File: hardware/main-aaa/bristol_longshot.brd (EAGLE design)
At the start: 14 x 50 mm, 57 parts, among them U1 SAM_D20E, U2 SI4060, U3 UBLOX_MAX, U4 ADP1607ACPZN-R7, U5 TG-5006CJ, U6 TG-5006CJ, U7 TPS3123, U8 SN74LVC1G32DCKR, U9 SE880, Y1 ABS05

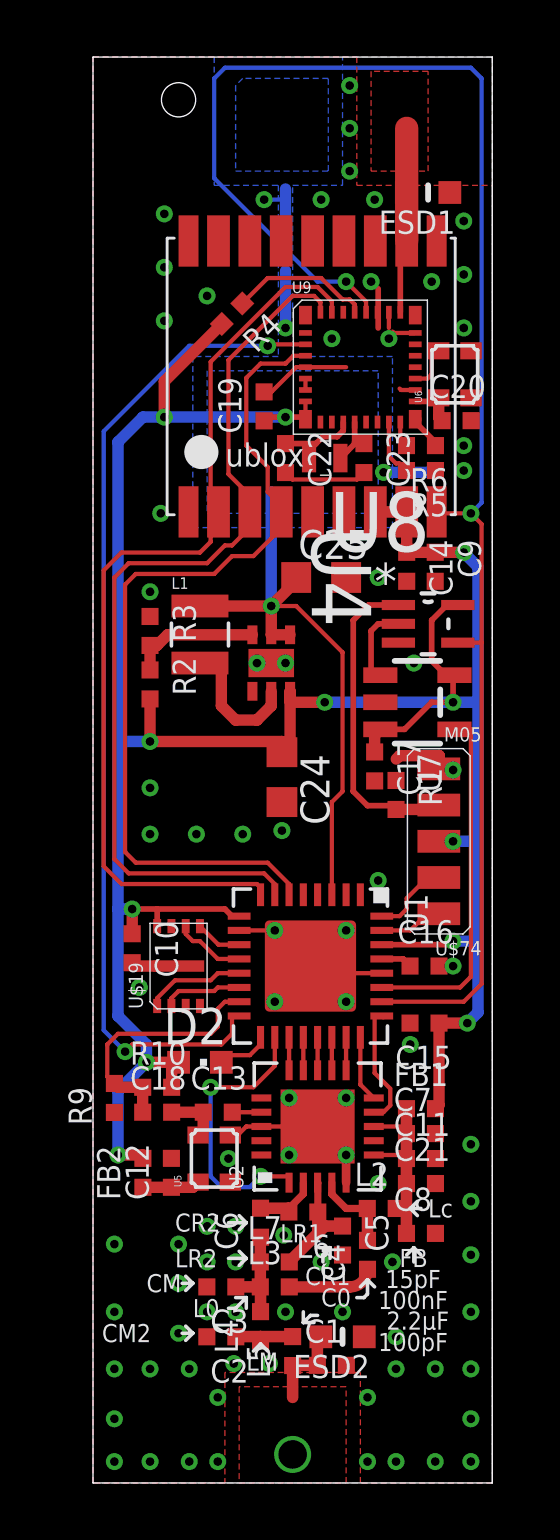
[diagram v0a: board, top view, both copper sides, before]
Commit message: Updated many parts lists, updated bard numbering, removed makefiles for inactive things
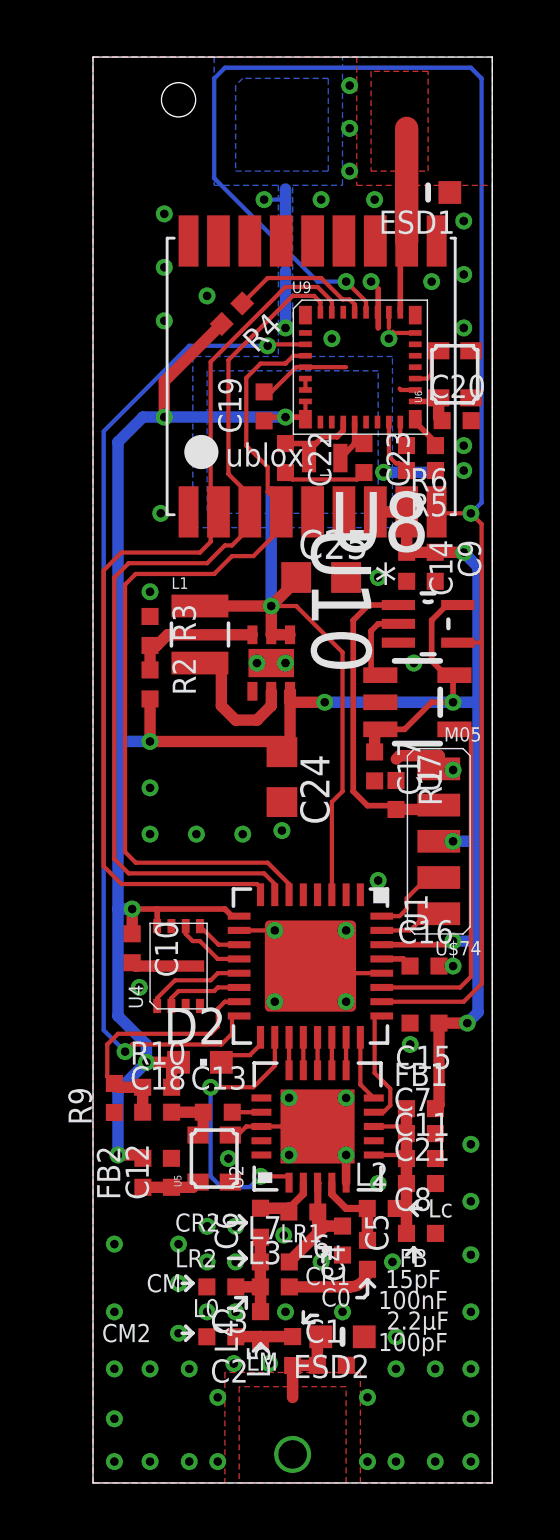
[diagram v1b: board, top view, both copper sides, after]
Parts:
- removed U$19: SST25WF040BT-40I/NP, fbri:USON-8
- added U10: ADP1607ACPZN-R7, ADP1607:DFN200X200X60-7N
- U4: value ADP1607ACPZN-R7 -> SST25WF040BT-40I/NP; device ADP1607:DFN200X200X60-7N -> fbri:USON-8
- moved U4 11.1 mm to (3.00, 18.1), turned to 0 degrees
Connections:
- net 1.2V: now also U10.1, U10.2; no longer U4.1, U4.2
- net 1.8V: now also U10.6, U4.8; no longer U$19.8, U4.6
- net FB: now also U10.3; no longer U4.3
- net GND: now also U10.4, U10.7, U4.P$9; no longer U$19.4, U$19.P$9, U4.7
- net MEM_CSN: now also U4.1; no longer U$19.1
- net MEM_MISO: now also U4.2; no longer U$19.2
- net MEM_MOSI: now also U4.5; no longer U$19.5
- net MEM_SCK: now also U4.6; no longer U$19.6
- net MEM_WPN: now also U4.3; no longer U$19.3
- net SW: now also U10.5; no longer U4.5
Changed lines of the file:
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@@
 <element name="C20" library="microbuilder_v3" package="_0402" value="100nF" x="12.75" y="37.25"/>
 <element name="C17" library="microbuilder_v3" package="_0402" value="100nF" x="9.875" y="25.125" rot="R270"/>
-<element name="U$19" library="fbri" package="USON-8" value="SST25WF040BT-40I/NP" x="3" y="18.125"/>
+<element name="U4" library="fbri" package="USON-8" value="SST25WF040BT-40I/NP" x="3" y="18.125"/>
 <element name="L1" library="SparkFun" package="1007" value="2.2µH" x="3.75" y="29.75"/>
 <element name="C24" library="resistor" package="C0603K" value="10µF" x="6.625" y="24.75" rot="R270"/>
-<element name="U4" library="ADP1607" package="DFN200X200X60-7N" value="ADP1607ACPZN-R7" x="6.25" y="28.75" rot="R270">
+<element name="U10" library="ADP1607" package="DFN200X200X60-7N" value="ADP1607ACPZN-R7" x="6.25" y="28.75" rot="R270">
 <attribute name="OC_FARNELL" value="2254940" x="51.25" y="39.75" size="1.778" layer="27" rot="R270" display="off"/>
 <attribute name="OC_NEWARK" value="54W6610" x="51.25" y="39.75" size="1.778" layer="27" rot="R270" display="off"/>
@@
 <via x="9" y="49" extent="1-16" drill="0.3"/>
 <via x="9" y="47.5" extent="1-16" drill="0.3"/>
-<contactref element="U$19" pad="4"/>
-<contactref element="U$19" pad="P$9"/>
+<contactref element="U4" pad="4"/>
+<contactref element="U4" pad="P$9"/>
 <via x="1.625" y="17.375" extent="1-16" drill="0.3"/>
 <wire x1="2.25" y1="18.125" x2="1.5" y2="18.125" width="0.4" layer="1"/>
 <wire x1="1.5" y1="18.125" x2="1.383" y2="18.242" width="0.4" layer="1"/>
 <wire x1="1.383" y1="18.242" x2="1.375" y2="18.242" width="0.4" layer="1"/>
-<contactref element="U4" pad="4"/>
+<contactref element="U10" pad="4"/>
 <contactref element="C24" pad="2"/>
-<contactref element="U4" pad="7"/>
+<contactref element="U10" pad="7"/>
 <contactref element="R3" pad="1"/>
 <contactref element="C25" pad="2"/>
@@
 <wire x1="9.875" y1="26.2251" x2="9.875" y2="25.633" width="0.4" layer="1"/>
 <via x="13" y="32.625" extent="1-16" drill="0.3"/>
-<contactref element="U$19" pad="8"/>
+<contactref element="U4" pad="8"/>
 <wire x1="1.375" y1="20.125" x2="2.25" y2="20.125" width="0.2" layer="1"/>
 <wire x1="2.25" y1="20.125" x2="4.625" y2="20.125" width="0.2" layer="1"/>
@@
 <wire x1="0.875" y1="13.75" x2="1.875" y2="14.75" width="0.4" layer="16"/>
 <contactref element="C24" pad="1"/>
-<contactref element="U4" pad="6"/>
+<contactref element="U10" pad="6"/>
 <contactref element="R2" pad="2"/>
 <via x="8.125" y="27.375" extent="1-16" drill="0.3"/>
@@
 </signal>
 <signal name="MEM_MOSI">
-<contactref element="U$19" pad="5"/>
+<contactref element="U4" pad="5"/>
 <contactref element="U1" pad="11"/>
 <wire x1="5.125" y1="18.875" x2="4.4" y2="18.875" width="0.15" layer="1"/>
@@
 </signal>
 <signal name="MEM_CSN">
-<contactref element="U$19" pad="1"/>
+<contactref element="U4" pad="1"/>
 <contactref element="U1" pad="13"/>
 <wire x1="5.125" y1="17.875" x2="4.375" y2="17.875" width="0.15" layer="1"/>
@@
 </signal>
 <signal name="MEM_SCK">
-<contactref element="U$19" pad="6"/>
+<contactref element="U4" pad="6"/>
 <contactref element="U1" pad="12"/>
 <wire x1="5.125" y1="18.375" x2="4.375" y2="18.375" width="0.15" layer="1"/>
@@
 </signal>
 <signal name="MEM_MISO">
-<contactref element="U$19" pad="2"/>
+<contactref element="U4" pad="2"/>
 <contactref element="U1" pad="14"/>
 <wire x1="5.125" y1="17.375" x2="4.375" y2="17.375" width="0.15" layer="1"/>
@@
 </signal>
 <signal name="MEM_WPN">
-<contactref element="U$19" pad="3"/>
+<contactref element="U4" pad="3"/>
 </signal>
 <signal name="RF_TANK">
@@
 </signal>
 <signal name="1.2V">
-<contactref element="U4" pad="1"/>
-<contactref element="U4" pad="2"/>
+<contactref element="U10" pad="1"/>
+<contactref element="U10" pad="2"/>
 <contactref element="L1" pad="1"/>
 <contactref element="C25" pad="1"/>
@@
 </signal>
 <signal name="SW">
-<contactref element="U4" pad="5"/>
+<contactref element="U10" pad="5"/>
 <contactref element="L1" pad="2"/>
 <wire x1="3.75" y1="28.75" x2="3.875" y2="28.625" width="0.4" layer="1"/>
@@
 </signal>
 <signal name="FB">
-<contactref element="U4" pad="3"/>
+<contactref element="U10" pad="3"/>
 <contactref element="R3" pad="2"/>
 <contactref element="R2" pad="1"/>

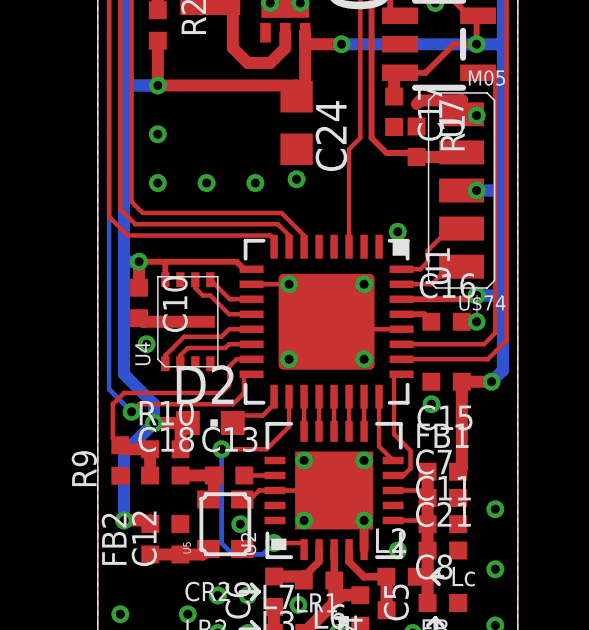
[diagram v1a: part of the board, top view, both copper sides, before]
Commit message: [Bugfix] Memory HOLD pin needs to be high. Also adjusted pad/cream size. Bump to V0.98x.1
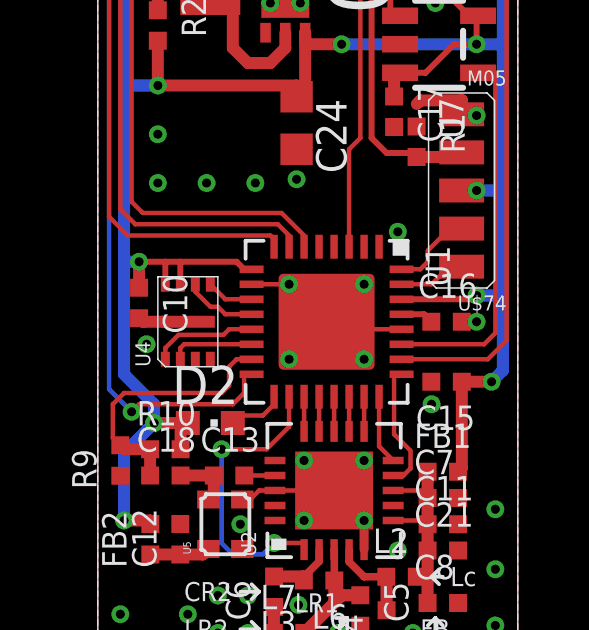
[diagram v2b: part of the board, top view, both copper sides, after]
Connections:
- net 1.8V: now also U4.7
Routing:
- net 1.8V: track 103.6 -> 104.5 mm
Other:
- board text added: "V0.982.1"
- board text removed: "V0.982.0"
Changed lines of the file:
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@@
 <wire x1="1.625" y1="48.875" x2="0.625" y2="49.375" width="0.2" layer="29" curve="-75"/>
 <wire x1="1.625" y1="41.875" x2="0.625" y2="41.375" width="0.2" layer="29"/>
-<text x="2.25" y="45.75" size="0.8" layer="29" font="vector" ratio="14">V0.982.0</text>
+<text x="2.25" y="45.75" size="0.8" layer="29" font="vector" ratio="14">V0.982.1</text>
 <rectangle x1="4.5" y1="45.5" x2="9" y2="49.5" layer="40"/>
 <rectangle x1="3.5" y1="33.5" x2="10.5" y2="39.5" layer="40"/>
@@
 <contactref element="U4" pad="8"/>
 <wire x1="1.375" y1="20.125" x2="2.25" y2="20.125" width="0.2" layer="1"/>
-<wire x1="2.25" y1="20.125" x2="4.625" y2="20.125" width="0.2" layer="1"/>
+<wire x1="2.25" y1="20.125" x2="2.75" y2="20.125" width="0.2" layer="1"/>
+<wire x1="2.75" y1="20.125" x2="4.625" y2="20.125" width="0.2" layer="1"/>
 <wire x1="4.625" y1="20.125" x2="4.875" y2="19.875" width="0.2" layer="1"/>
 <wire x1="4.875" y1="19.875" x2="5.125" y2="19.875" width="0.2" layer="1"/>
-<wire x1="2.25" y1="19.525" x2="2.25" y2="20.125" width="0.2" layer="1"/>
+<wire x1="2.25" y1="19.375" x2="2.25" y2="20.125" width="0.2" layer="1"/>
 <wire x1="1.375" y1="19.258" x2="1.375" y2="20.125" width="0.4" layer="1"/>
 <wire x1="2.5" y1="38.625" x2="4.5157875" y2="40.6407875" width="0.4" layer="1"/>
@@
 <wire x1="2" y1="26" x2="6.625" y2="26" width="0.4" layer="1"/>
 <wire x1="6.625" y1="26" x2="6.625" y2="25.625" width="0.4" layer="1"/>
+<contactref element="U4" pad="7"/>
+<wire x1="2.75" y1="19.375" x2="2.75" y2="20.125" width="0.2" layer="1"/>
 </signal>
 <signal name="VDD_CORE">
@@
 <contactref element="U4" pad="5"/>
 <contactref element="U1" pad="11"/>
-<wire x1="5.125" y1="18.875" x2="4.4" y2="18.875" width="0.15" layer="1"/>
-<wire x1="4.4" y1="18.875" x2="3.75" y2="19.525" width="0.15" layer="1"/>
+<wire x1="5.125" y1="18.875" x2="4.25" y2="18.875" width="0.15" layer="1"/>
+<wire x1="4.25" y1="18.875" x2="3.75" y2="19.375" width="0.15" layer="1"/>
 </signal>
 <signal name="MEM_CSN">
@@
 <contactref element="U1" pad="13"/>
 <wire x1="5.125" y1="17.875" x2="4.375" y2="17.875" width="0.15" layer="1"/>
-<wire x1="4.375" y1="17.875" x2="4.125" y2="17.625" width="0.15" layer="1"/>
-<wire x1="4.125" y1="17.625" x2="2.875" y2="17.625" width="0.15" layer="1"/>
-<wire x1="2.875" y1="17.625" x2="2.25" y2="17" width="0.15" layer="1"/>
-<wire x1="2.25" y1="17" x2="2.25" y2="16.725" width="0.15" layer="1"/>
+<wire x1="4.375" y1="17.875" x2="4.1875" y2="17.6875" width="0.15" layer="1"/>
+<wire x1="4.1875" y1="17.6875" x2="2.6875" y2="17.6875" width="0.15" layer="1"/>
+<wire x1="2.6875" y1="17.6875" x2="2.25" y2="17.25" width="0.15" layer="1"/>
+<wire x1="2.25" y1="17.25" x2="2.25" y2="16.875" width="0.15" layer="1"/>
 </signal>
 <signal name="GIMO">
@@
 <contactref element="U4" pad="6"/>
 <contactref element="U1" pad="12"/>
-<wire x1="5.125" y1="18.375" x2="4.375" y2="18.375" width="0.15" layer="1"/>
-<wire x1="4.375" y1="18.375" x2="3.75" y2="19" width="0.15" layer="1"/>
-<wire x1="3.75" y1="19" x2="3.5" y2="19" width="0.15" layer="1"/>
-<wire x1="3.5" y1="19" x2="3.25" y2="19.25" width="0.15" layer="1"/>
-<wire x1="3.25" y1="19.25" x2="3.25" y2="19.525" width="0.15" layer="1"/>
+<wire x1="5.125" y1="18.375" x2="4.25" y2="18.375" width="0.15" layer="1"/>
+<wire x1="4.25" y1="18.375" x2="4" y2="18.625" width="0.15" layer="1"/>
+<wire x1="4" y1="18.625" x2="3.75" y2="18.625" width="0.15" layer="1"/>
+<wire x1="3.75" y1="18.625" x2="3.25" y2="19.125" width="0.15" layer="1"/>
+<wire x1="3.25" y1="19.125" x2="3.25" y2="19.375" width="0.15" layer="1"/>
 </signal>
 <signal name="MEM_MISO">
 <contactref element="U4" pad="2"/>
 <contactref element="U1" pad="14"/>
-<wire x1="5.125" y1="17.375" x2="4.375" y2="17.375" width="0.15" layer="1"/>
-<wire x1="4.375" y1="17.375" x2="4.25" y2="17.25" width="0.15" layer="1"/>
-<wire x1="4.25" y1="17.25" x2="3" y2="17.25" width="0.15" layer="1"/>
-<wire x1="3" y1="17.25" x2="2.75" y2="17" width="0.15" layer="1"/>
-<wire x1="2.75" y1="17" x2="2.75" y2="16.725" width="0.15" layer="1"/>
+<wire x1="5.125" y1="17.375" x2="2.875" y2="17.375" width="0.15" layer="1"/>
+<wire x1="2.875" y1="17.375" x2="2.75" y2="17.25" width="0.15" layer="1"/>
+<wire x1="2.75" y1="17.25" x2="2.75" y2="16.875" width="0.15" layer="1"/>
 </signal>
 <signal name="SI_MOSI">

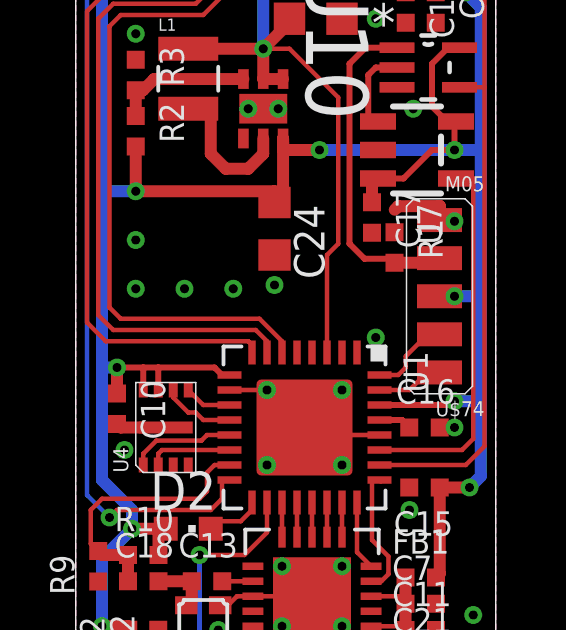
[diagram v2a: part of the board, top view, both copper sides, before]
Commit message: Added vias though all the pads on the debug connector
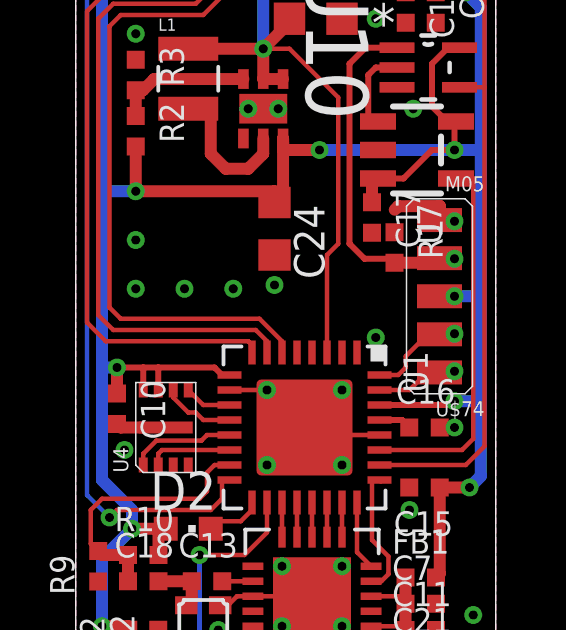
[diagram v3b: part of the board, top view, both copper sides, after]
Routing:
- net SWDCLK: track 2.24 -> 2.78 mm, vias 0 -> 1
- net SWDIO: track 2.78 -> 3.30 mm, vias 0 -> 1
- net EXT!RESET: track 11.1 -> 11.7 mm, vias 0 -> 1
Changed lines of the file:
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@@
 <wire x1="11.625" y1="21.125" x2="12.02" y2="21.125" width="0.15" layer="1"/>
 <wire x1="12.02" y1="21.125" x2="12.125" y2="21.23" width="0.15" layer="1"/>
+<via x="12.625" y="21.25" extent="1-16" drill="0.3"/>
+<wire x1="12.125" y1="21.23" x2="12.625" y2="21.23" width="0.2" layer="1"/>
+<wire x1="12.625" y1="21.23" x2="12.625" y2="21.25" width="0.2" layer="1"/>
 </signal>
 <signal name="SWDCLK">
@@
 <wire x1="11.5" y1="19.75" x2="11.915" y2="19.75" width="0.15" layer="1"/>
 <wire x1="11.915" y1="19.75" x2="12.125" y2="19.96" width="0.15" layer="1"/>
+<via x="12.625" y="20" extent="1-16" drill="0.3"/>
+<wire x1="12.125" y1="19.96" x2="12.125" y2="20" width="0.2" layer="1"/>
+<wire x1="12.125" y1="20" x2="12.625" y2="20" width="0.2" layer="1"/>
 </signal>
 <signal name="KEY">
@@
 <wire x1="9.625" y1="23.75" x2="10.492" y2="23.75" width="0.2" layer="1"/>
 <wire x1="10.492" y1="23.75" x2="10.625" y2="23.617" width="0.2" layer="1"/>
+<via x="12.625" y="23.75" extent="1-16" drill="0.3"/>
+<wire x1="12.625" y1="23.75" x2="12.125" y2="23.75" width="0.2" layer="1"/>
+<wire x1="12.125" y1="23.75" x2="12.125" y2="23.77" width="0.2" layer="1"/>
 </signal>
 <signal name="SAM_XOSC">
